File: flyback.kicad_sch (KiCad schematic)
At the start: 47 parts, among them Q2001 FDC86244, U2001 TPS23751PWP, U2002 TCMT1107, U2003 TLV431ACDBZR

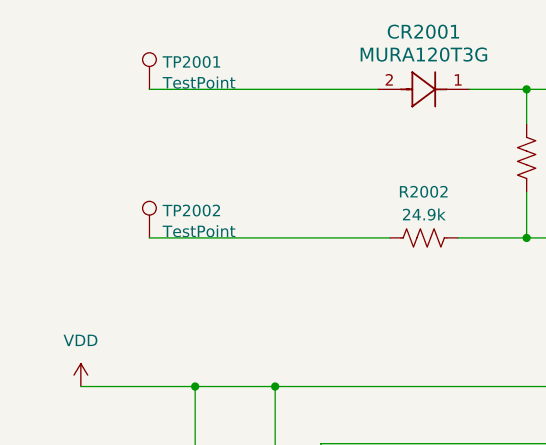
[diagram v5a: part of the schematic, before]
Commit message: Changed all passive footprints to 0805
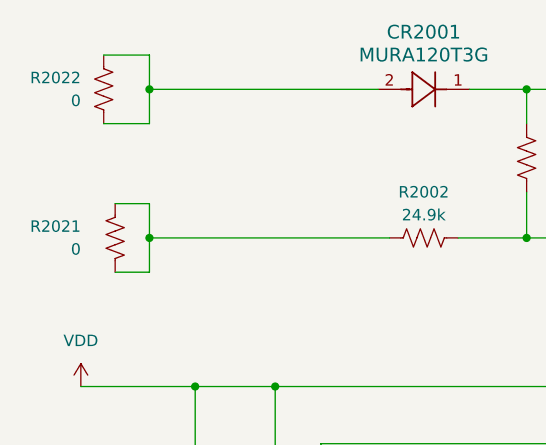
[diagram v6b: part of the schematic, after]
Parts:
- removed TP2001, TP2002: TestPoint, SparkFun-Connector:TestPoint-1.0mm, symbol Connector:TestPoint
- added R2021: 0, Resistor_SMD:R_0805_2012Metric, symbol SparkFun-Resistor:0.47_0603
- added R2022: 0, Resistor_SMD:R_0805_2012Metric, symbol Device:R_US
- C2001, C2004, C2008, C2010, C2013, C2014: footprint SparkFun-Capacitor:C_0402_1005Metric -> Capacitor_SMD:C_0805_2012Metric
- C2011: footprint Capacitor_SMD:C_0402_1005Metric -> Capacitor_SMD:C_0805_2012Metric
- C2012: footprint Capacitor_SMD:C_0603_1608Metric -> Capacitor_SMD:C_0805_2012Metric
- R2001, R2003, R2012, R2013, R2014, R2015, R2016, R2017, R2018, R2019, R2020: footprint Resistor_SMD:R_0402_1005Metric -> Resistor_SMD:R_0805_2012Metric
- R2002: footprint Resistor_SMD:R_01005_0402Metric -> Resistor_SMD:R_0805_2012Metric
- R2004, R2005, R2006, R2007, R2008, R2009, R2010: footprint Resistor_SMD:R_01005_0402Metric -> LED_SMD:LED_0805_2012Metric
- R2011: footprint Resistor_SMD:R_0603_1608Metric -> Resistor_SMD:R_0805_2012Metric
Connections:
- net at CR2001.2: now also R2022.1, R2022.2
- net at R2002.2: now also R2021.1, R2021.2

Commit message: Starting Layout
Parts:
- renumbered R2022 to R2001, R2001 to R2002, R2021 to R2003, R2002 to R2004, R2003 to R2005, R2004 to R2006, R2005 to R2007, R2006 to R2008, R2007 to R2009, R2008 to R2010, R2009 to R2011, R2010 to R2012, R2011 to R2013, R2012 to R2014, R2013 to R2015, R2014 to R2016, R2015 to R2017, R2016 to R2018, R2017 to R2019, R2018 to R2020, R2019 to R2021, R2020 to R2022
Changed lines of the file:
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@@
 		)
 	)
+	(global_label "T2P"
+		(shape input)
+		(at 107.95 81.28 0)
+		(fields_autoplaced yes)
+		(effects
+			(font
+				(size 1.27 1.27)
+			)
+			(justify left)
+		)
+		(property "Intersheetrefs" "${INTERSHEET_REFS}"
+			(at 114.3823 81.28 0)
+			(effects
+				(font
+					(size 1.27 1.27)
+				)
+				(justify left)
+				(hide yes)
+			)
+		)
+	)
 	(symbol
 		(lib_id "MBRS540T3G:MBRS540T3G")
@@
 		(dnp no)
 		(fields_autoplaced yes)
-		(property "Reference" "R2008"
+		(property "Reference" "R2010"
 			(at 187.96 92.71 90)
 			(effects
@@
 			(project "PoE"
 				(path "/e8d70991-5081-4afb-b8c3-5ce9f62355e0/1fdbb5e2-ecd4-47ea-a63c-f2f18c06d291"
-					(reference "R2008")
+					(reference "R2010")
 					(unit 1)
 				)
@@
 		(on_board yes)
 		(dnp no)
-		(property "Reference" "R2012"
+		(property "Reference" "R2014"
 			(at 48.26 116.8399 0)
 			(effects
@@
 			(project "PoE"
 				(path "/e8d70991-5081-4afb-b8c3-5ce9f62355e0/1fdbb5e2-ecd4-47ea-a63c-f2f18c06d291"
-					(reference "R2012")
+					(reference "R2014")
 					(unit 1)
 				)
@@
 		(dnp no)
 		(fields_autoplaced yes)
-		(property "Reference" "R2004"
+		(property "Reference" "R2006"
 			(at 39.37 67.3099 0)
 			(effects
@@
 			(project ""
 				(path "/e8d70991-5081-4afb-b8c3-5ce9f62355e0/1fdbb5e2-ecd4-47ea-a63c-f2f18c06d291"
-					(reference "R2004")
+					(reference "R2006")
 					(unit 1)
 				)
@@
 		(dnp no)
 		(fields_autoplaced yes)
-		(property "Reference" "R2013"
+		(property "Reference" "R2015"
 			(at 60.96 116.8399 0)
 			(effects
@@
 			(project "PoE"
 				(path "/e8d70991-5081-4afb-b8c3-5ce9f62355e0/1fdbb5e2-ecd4-47ea-a63c-f2f18c06d291"
-					(reference "R2013")
+					(reference "R2015")
 					(unit 1)
 				)
@@
 		(on_board yes)
 		(dnp no)
-		(property "Reference" "R2010"
+		(property "Reference" "R2012"
 			(at 48.26 106.6799 0)
 			(effects
@@
 			(project "PoE"
 				(path "/e8d70991-5081-4afb-b8c3-5ce9f62355e0/1fdbb5e2-ecd4-47ea-a63c-f2f18c06d291"
-					(reference "R2010")
+					(reference "R2012")
 					(unit 1)
 				)
@@
 		(dnp no)
 		(fields_autoplaced yes)
-		(property "Reference" "R2001"
+		(property "Reference" "R2002"
 			(at 76.2 30.4799 0)
 			(effects
@@
 			(project "PoE"
 				(path "/e8d70991-5081-4afb-b8c3-5ce9f62355e0/1fdbb5e2-ecd4-47ea-a63c-f2f18c06d291"
-					(reference "R2001")
+					(reference "R2002")
 					(unit 1)
 				)
@@
 		(dnp no)
 		(fields_autoplaced yes)
-		(property "Reference" "R2019"
+		(property "Reference" "R2021"
 			(at 265.43 148.5899 0)
 			(effects
@@
 			(project "PoE"
 				(path "/e8d70991-5081-4afb-b8c3-5ce9f62355e0/1fdbb5e2-ecd4-47ea-a63c-f2f18c06d291"
-					(reference "R2019")
+					(reference "R2021")
 					(unit 1)
 				)
@@
 		(on_board yes)
 		(dnp no)
-		(property "Reference" "R2021"
+		(property "Reference" "R2003"
 			(at 24.13 39.3699 90)
 			(effects
@@
 			(project ""
 				(path "/e8d70991-5081-4afb-b8c3-5ce9f62355e0/1fdbb5e2-ecd4-47ea-a63c-f2f18c06d291"
-					(reference "R2021")
+					(reference "R2003")
 					(unit 1)
 				)
@@
 		(dnp no)
 		(fields_autoplaced yes)
-		(property "Reference" "R2017"
+		(property "Reference" "R2019"
 			(at 111.76 133.35 90)
 			(effects
@@
 			(project "PoE"
 				(path "/e8d70991-5081-4afb-b8c3-5ce9f62355e0/1fdbb5e2-ecd4-47ea-a63c-f2f18c06d291"
-					(reference "R2017")
+					(reference "R2019")
 					(unit 1)
 				)
@@
 		(dnp no)
 		(fields_autoplaced yes)
-		(property "Reference" "R2003"
+		(property "Reference" "R2005"
 			(at 168.91 62.2299 0)
 			(effects
@@
 			(project "PoE"
 				(path "/e8d70991-5081-4afb-b8c3-5ce9f62355e0/1fdbb5e2-ecd4-47ea-a63c-f2f18c06d291"
-					(reference "R2003")
+					(reference "R2005")
 					(unit 1)
 				)
@@
 		(dnp no)
 		(fields_autoplaced yes)
-		(property "Reference" "R2002"
+		(property "Reference" "R2004"
 			(at 62.23 35.56 90)
 			(effects
@@
 			(project "PoE"
 				(path "/e8d70991-5081-4afb-b8c3-5ce9f62355e0/1fdbb5e2-ecd4-47ea-a63c-f2f18c06d291"
-					(reference "R2002")
+					(reference "R2004")
 					(unit 1)
 				)
@@
 		(on_board yes)
 		(dnp no)
-		(property "Reference" "R2007"
+		(property "Reference" "R2009"
 			(at 29.21 96.5199 0)
 			(effects
@@
 			(project ""
 				(path "/e8d70991-5081-4afb-b8c3-5ce9f62355e0/1fdbb5e2-ecd4-47ea-a63c-f2f18c06d291"
-					(reference "R2007")
+					(reference "R2009")
 					(unit 1)
 				)
@@
 		(on_board yes)
 		(dnp no)
-		(property "Reference" "R2011"
+		(property "Reference" "R2013"
 			(at 211.328 108.458 0)
 			(effects
@@
 			(project "PoE"
 				(path "/e8d70991-5081-4afb-b8c3-5ce9f62355e0/1fdbb5e2-ecd4-47ea-a63c-f2f18c06d291"
-					(reference "R2011")
+					(reference "R2013")
 					(unit 1)
 				)
@@
 		(dnp no)
 		(fields_autoplaced yes)
-		(property "Reference" "R2020"
+		(property "Reference" "R2022"
 			(at 157.48 152.3999 0)
 			(effects
@@
 			(project "PoE"
 				(path "/e8d70991-5081-4afb-b8c3-5ce9f62355e0/1fdbb5e2-ecd4-47ea-a63c-f2f18c06d291"
-					(reference "R2020")
+					(reference "R2022")
 					(unit 1)
 				)
@@
 		(dnp no)
 		(fields_autoplaced yes)
-		(property "Reference" "R2016"
+		(property "Reference" "R2018"
 			(at 219.71 129.54 90)
 			(effects
@@
 			(project "PoE"
 				(path "/e8d70991-5081-4afb-b8c3-5ce9f62355e0/1fdbb5e2-ecd4-47ea-a63c-f2f18c06d291"
-					(reference "R2016")
+					(reference "R2018")
 					(unit 1)
 				)
@@
 		(dnp no)
 		(fields_autoplaced yes)
-		(property "Reference" "R2018"
+		(property "Reference" "R2020"
 			(at 111.76 143.51 90)
 			(effects
@@
 			(project "PoE"
 				(path "/e8d70991-5081-4afb-b8c3-5ce9f62355e0/1fdbb5e2-ecd4-47ea-a63c-f2f18c06d291"
-					(reference "R2018")
+					(reference "R2020")
 					(unit 1)
 				)
@@
 		(dnp no)
 		(fields_autoplaced yes)
-		(property "Reference" "R2014"
+		(property "Reference" "R2016"
 			(at 198.12 119.3799 0)
 			(effects
@@
 			(project "PoE"
 				(path "/e8d70991-5081-4afb-b8c3-5ce9f62355e0/1fdbb5e2-ecd4-47ea-a63c-f2f18c06d291"
-					(reference "R2014")
+					(reference "R2016")
 					(unit 1)
 				)
@@
 		(dnp no)
 		(fields_autoplaced yes)
-		(property "Reference" "R2005"
+		(property "Reference" "R2007"
 			(at 132.08 73.6599 0)
 			(effects
@@
 			(project "PoE"
 				(path "/e8d70991-5081-4afb-b8c3-5ce9f62355e0/1fdbb5e2-ecd4-47ea-a63c-f2f18c06d291"
-					(reference "R2005")
+					(reference "R2007")
 					(unit 1)
 				)
@@
 		(dnp no)
 		(fields_autoplaced yes)
-		(property "Reference" "R2006"
+		(property "Reference" "R2008"
 			(at 176.53 82.55 90)
 			(effects
@@
 			(project "PoE"
 				(path "/e8d70991-5081-4afb-b8c3-5ce9f62355e0/1fdbb5e2-ecd4-47ea-a63c-f2f18c06d291"
-					(reference "R2006")
+					(reference "R2008")
 					(unit 1)
 				)
@@
 		(dnp no)
 		(fields_autoplaced yes)
-		(property "Reference" "R2009"
+		(property "Reference" "R2011"
 			(at 166.37 97.79 90)
 			(effects
@@
 			(project "PoE"
 				(path "/e8d70991-5081-4afb-b8c3-5ce9f62355e0/1fdbb5e2-ecd4-47ea-a63c-f2f18c06d291"
-					(reference "R2009")
+					(reference "R2011")
 					(unit 1)
 				)
@@
 		(on_board yes)
 		(dnp no)
-		(property "Reference" "R2022"
+		(property "Reference" "R2001"
 			(at 24.13 22.8599 0)
 			(effects
@@
 			(project ""
 				(path "/e8d70991-5081-4afb-b8c3-5ce9f62355e0/1fdbb5e2-ecd4-47ea-a63c-f2f18c06d291"
-					(reference "R2022")
+					(reference "R2001")
 					(unit 1)
 				)
@@
 		(dnp no)
 		(fields_autoplaced yes)
-		(property "Reference" "R2015"
+		(property "Reference" "R2017"
 			(at 265.43 128.2699 0)
 			(effects
@@
 			(project "PoE"
 				(path "/e8d70991-5081-4afb-b8c3-5ce9f62355e0/1fdbb5e2-ecd4-47ea-a63c-f2f18c06d291"
-					(reference "R2015")
+					(reference "R2017")
 					(unit 1)
 				)
